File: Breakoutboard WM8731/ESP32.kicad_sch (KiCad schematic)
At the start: 23 parts

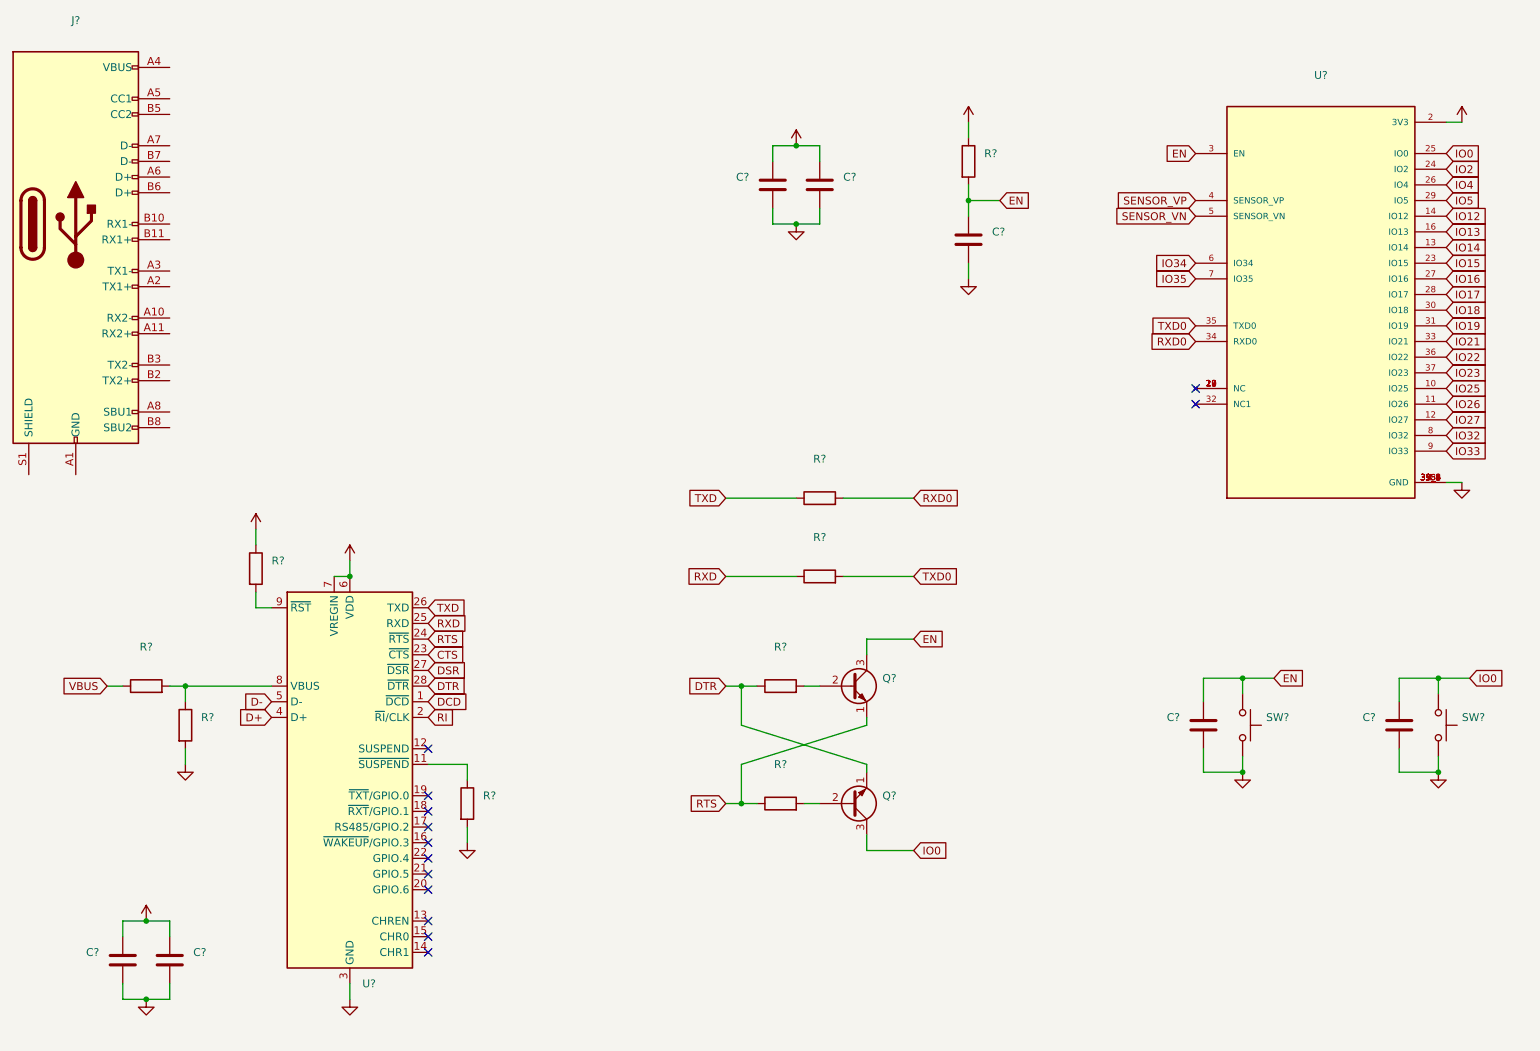
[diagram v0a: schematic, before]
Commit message: Changed WM8731 breakout board structure and header pins
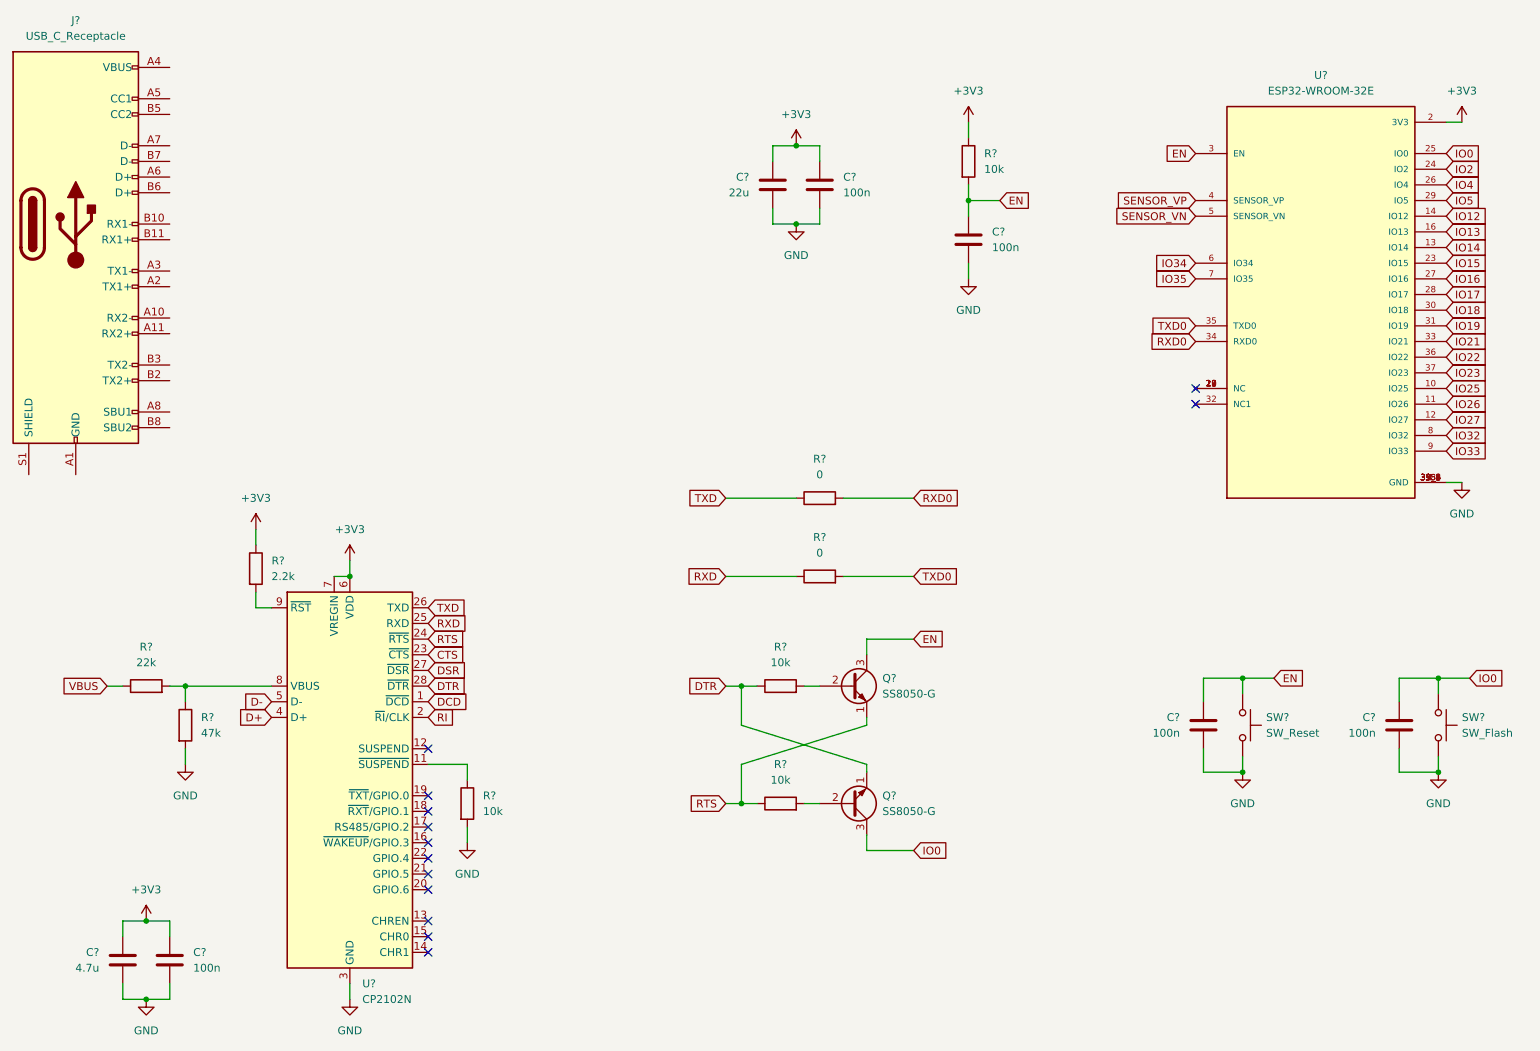
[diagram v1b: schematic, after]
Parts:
- C? (x5): value (none) -> 100n
- C?: value (none) -> 22u
- C?: value (none) -> 4.7u
- J?: value (none) -> USB_C_Receptacle
- Q? (x2): value (none) -> SS8050-G; footprint (none) -> Package_TO_SOT_THT:TO-92_Inline
- R?: value (none) -> 2.2k
- R?: value (none) -> 22k
- R? (x4): value (none) -> 10k
- R?: value (none) -> 47k
- R? (x2): value (none) -> 0
- SW?: value (none) -> SW_Reset
- SW?: value (none) -> SW_Flash
- U?: value (none) -> CP2102N; footprint (none) -> Package_DFN_QFN:QFN-28-1EP_5x5mm_P0.5mm_EP3.35x3.35mm
- U?: value (none) -> ESP32-WROOM-32E; footprint (none) -> XCVR_ESP32-WROOM-32E_(16MB)
